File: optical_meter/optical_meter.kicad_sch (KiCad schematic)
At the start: 45 parts, among them J1 SFP+, J2 SFP+, J3 Conn_01x02_Pin, U2 FIN1002M5X, U3 FIN1001M5X

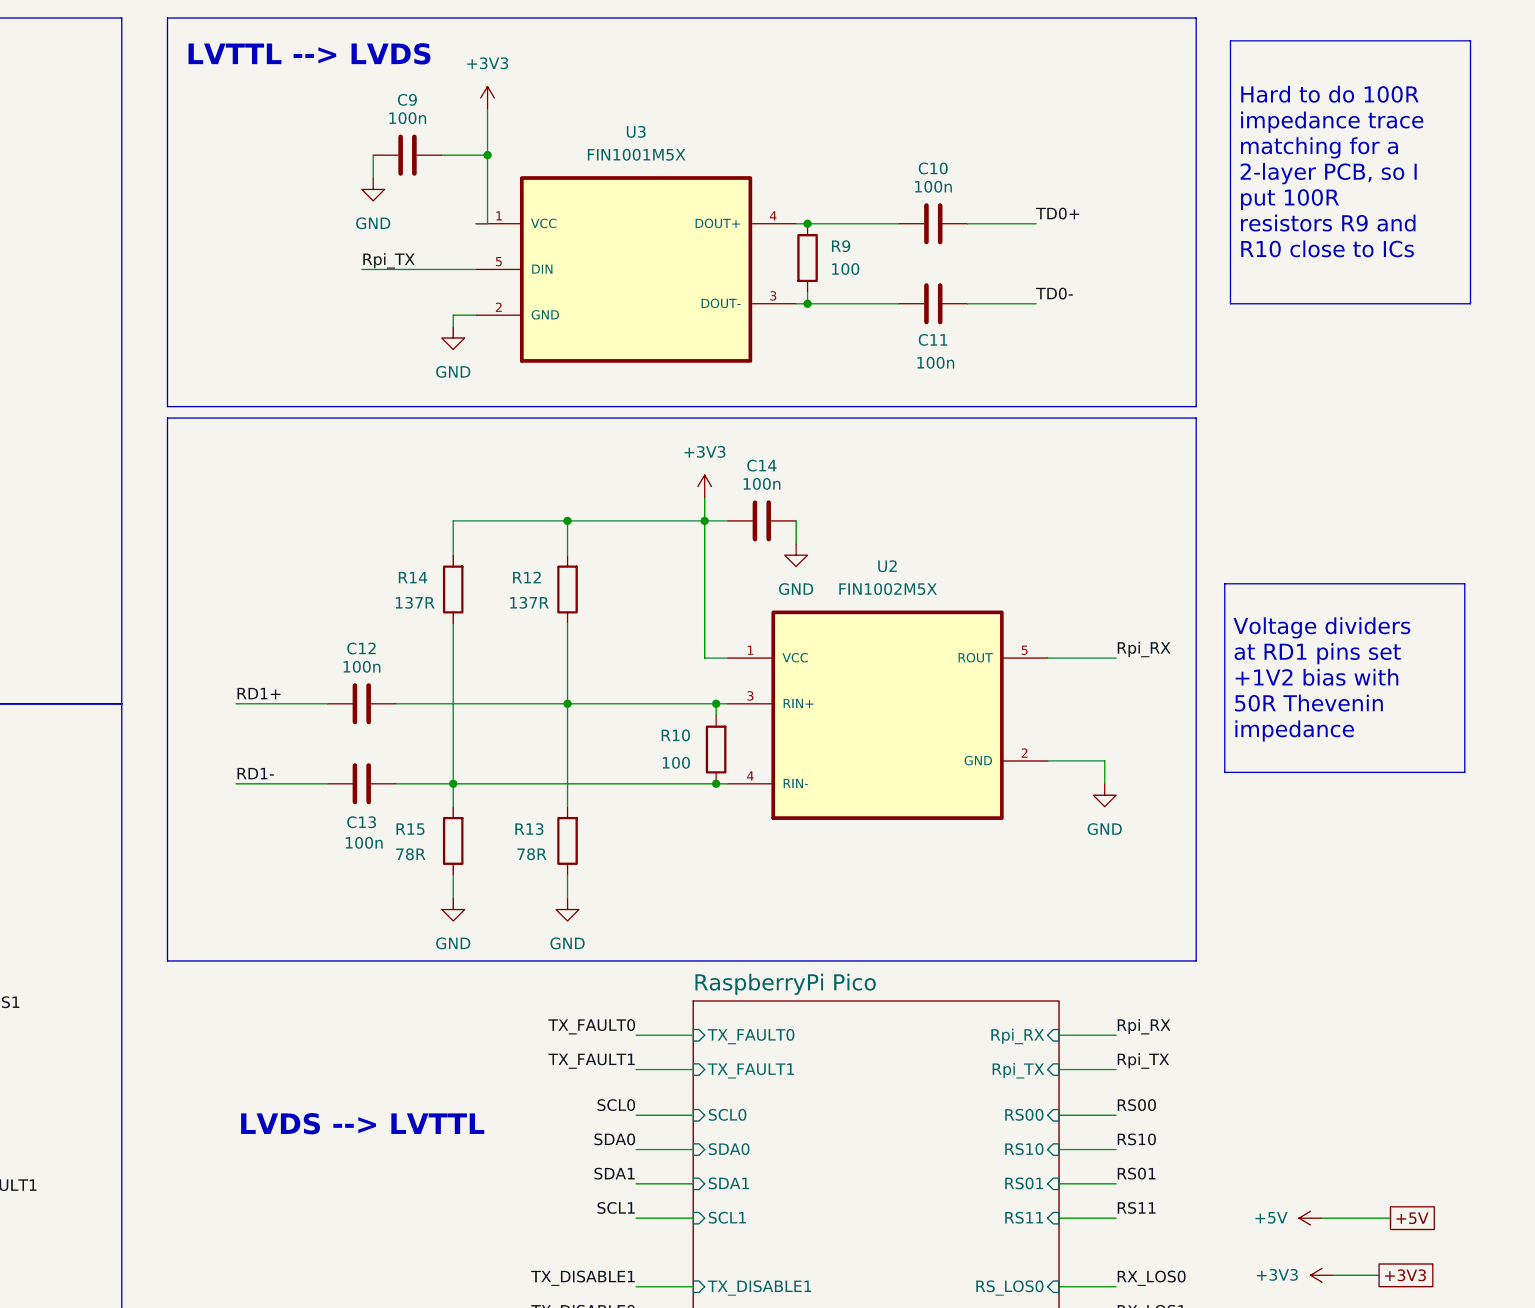
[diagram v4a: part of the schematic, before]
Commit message: Removing 100R termination Resistor R9 from TD0 lines
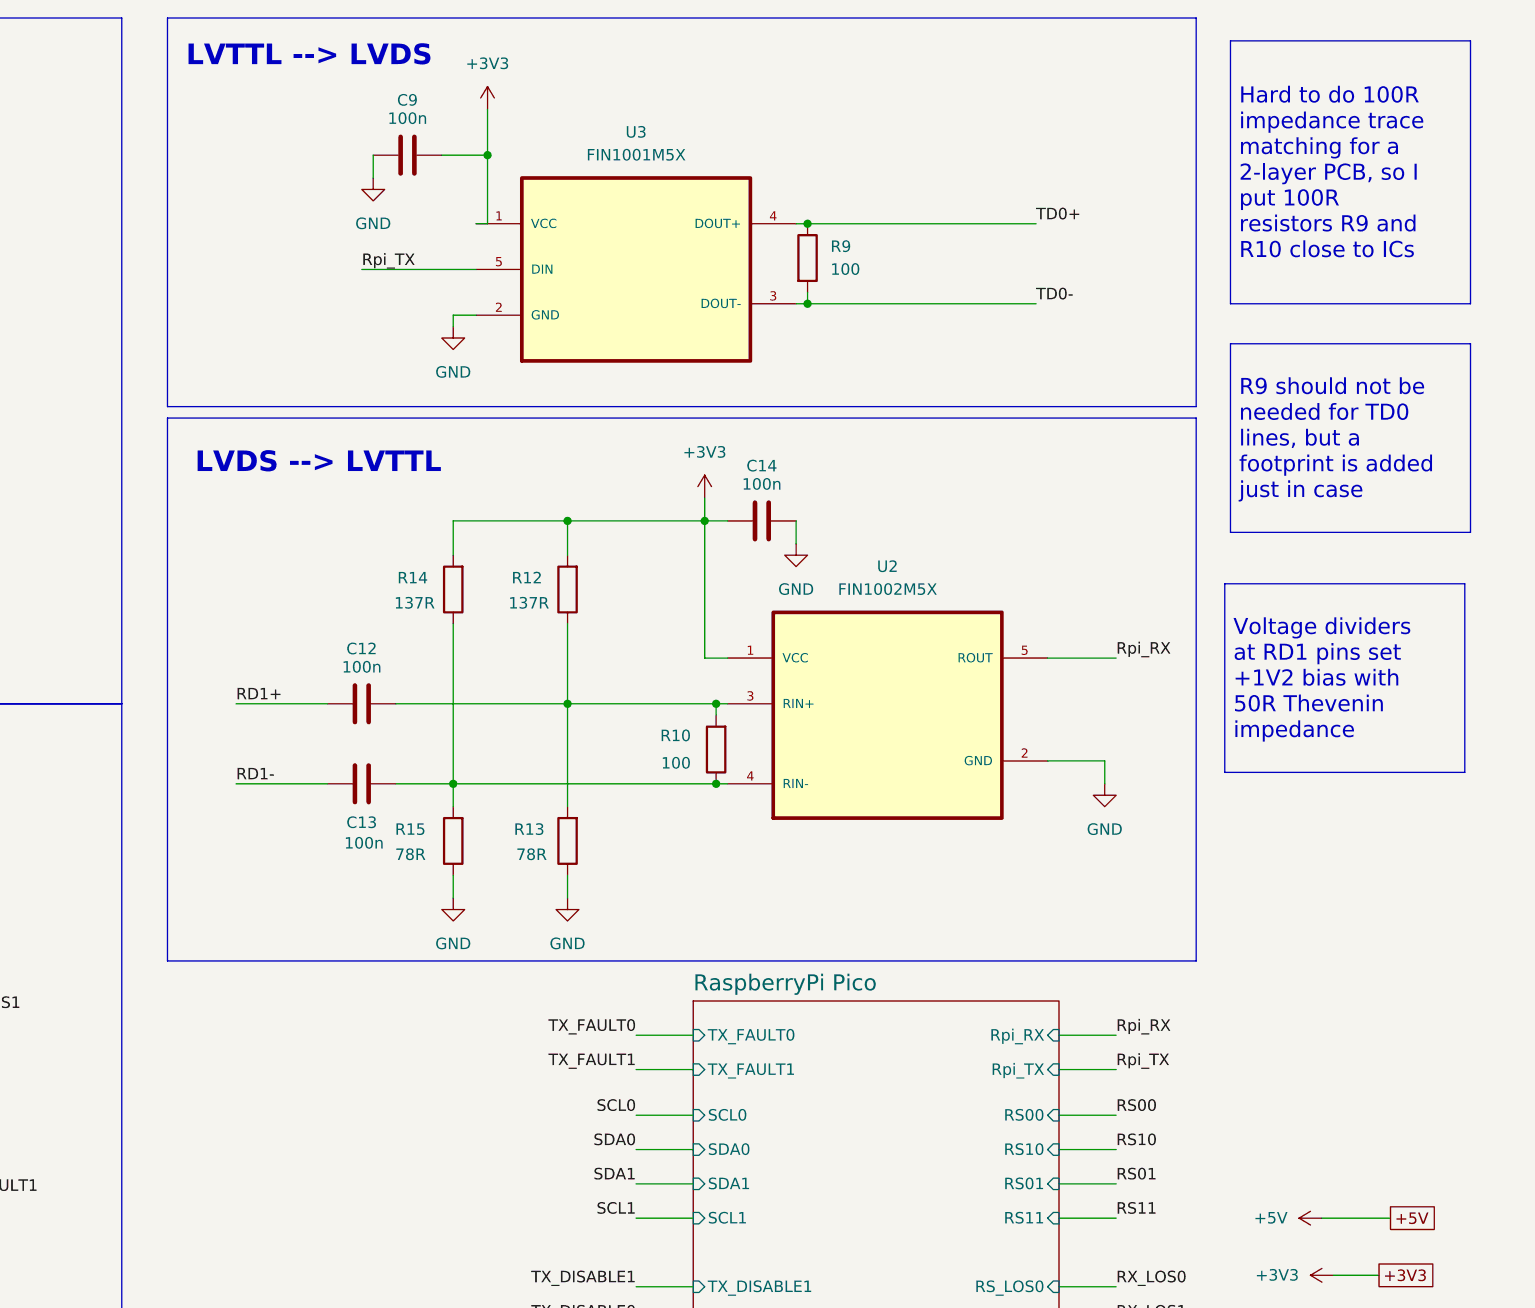
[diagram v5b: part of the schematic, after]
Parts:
- removed C10, C11: 100n, Capacitor_SMD:C_0603_1608Metric, symbol Device:C
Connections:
- net TD0+: now also R9.1, U3.4 (DOUT+)
- net TD0-: now also R9.2, U3.3 (DOUT-)
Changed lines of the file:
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@@
 	(text "LVDS --> LVTTL"
 		(exclude_from_sim no)
-		(at 158.75 135.89 0)
+		(at 153.924 62.23 0)
 		(effects
 			(font
@@
 		)
 	)
+	(text_box "R9 should not be needed for TD0 lines, but a footprint is added just in case"
+		(exclude_from_sim no)
+		(at 255.27 48.895 0)
+		(size 26.67 20.955)
+		(margins 0.9525 0.9525 0.9525 0.9525)
+		(stroke
+			(width 0)
+			(type solid)
+		)
+		(fill
+			(type color)
+			(color 241 253 255 1)
+		)
+		(effects
+			(font
+				(size 1.778 1.778)
+			)
+			(justify left)
+		)
+	)
 	(junction
 		(at 49.53 143.51)
@@
 	(wire
 		(pts
-			(xy 208.28 44.45) (xy 218.44 44.45)
+			(xy 208.28 44.45) (xy 233.68 44.45)
 		)
 		(stroke
@@
 	(wire
 		(pts
-			(xy 226.06 35.56) (xy 233.68 35.56)
-		)
-		(stroke
-			(width 0)
-			(type default)
-		)
-	)
-	(wire
-		(pts
 			(xy 54.61 97.79) (xy 54.61 102.87)
 		)
@@
 	(wire
 		(pts
-			(xy 208.28 35.56) (xy 218.44 35.56)
+			(xy 208.28 35.56) (xy 233.68 35.56)
 		)
 		(stroke
@@
 		)
 	)
-	(wire
-		(pts
-			(xy 226.06 44.45) (xy 233.68 44.45)
-		)
-		(stroke
-			(width 0)
-			(type default)
-		)
-	)
 	(label "RS00"
 		(at 46.99 64.77 0)
@@
 		(at 208.28 39.37 0)
 		(unit 1)
-		(exclude_from_sim no)
+		(exclude_from_sim yes)
 		(in_bom yes)
-		(on_board yes)
+		(on_board no)
 		(dnp no)
 		(fields_autoplaced yes)
@@
 	)
 	(symbol
-		(lib_id "Device:C")
-		(at 222.25 44.45 90)
-		(unit 1)
-		(exclude_from_sim no)
-		(in_bom yes)
-		(on_board yes)
-		(dnp no)
-		(property "Reference" "C11"
-			(at 222.25 48.514 90)
-			(effects
-				(font
-					(size 1.27 1.27)
-				)
-			)
-		)
-		(property "Value" "100n"
-			(at 222.504 51.054 90)
-			(effects
-				(font
-					(size 1.27 1.27)
-				)
-			)
-		)
-		(property "Footprint" "Capacitor_SMD:C_0603_1608Metric"
-			(at 226.06 43.4848 0)
-			(effects
-				(font
-					(size 1.27 1.27)
-				)
-				(hide yes)
-			)
-		)
-		(property "Datasheet" "~"
-			(at 222.25 44.45 0)
-			(effects
-				(font
-					(size 1.27 1.27)
-				)
-				(hide yes)
-			)
-		)
-		(property "Description" "Unpolarized capacitor"
-			(at 222.25 44.45 0)
-			(effects
-				(font
-					(size 1.27 1.27)
-				)
-				(hide yes)
-			)
-		)
-		(pin "1"
-		)
-		(pin "2"
-		)
-		(instances
-			(project "optical_meter"
-				(path "/329e6fb6-763d-4479-a593-6f78470800a1"
-					(reference "C11")
-					(unit 1)
-				)
-			)
-		)
-	)
-	(symbol
 		(lib_id "Device:LED")
 		(at 81.28 189.23 180)
@@
 					(unit 1)
 				)
-			)
-		)
-	)
-	(symbol
-		(lib_id "Device:C")
-		(at 222.25 35.56 90)
-		(unit 1)
-		(exclude_from_sim no)
-		(in_bom yes)
-		(on_board yes)
-		(dnp no)
-		(property "Reference" "C10"
-			(at 222.25 29.464 90)
-			(effects
-				(font
-					(size 1.27 1.27)
-				)
-			)
-		)
-		(property "Value" "100n"
-			(at 222.25 31.496 90)
-			(effects
-				(font
-					(size 1.27 1.27)
-				)
-			)
-		)
-		(property "Footprint" "Capacitor_SMD:C_0603_1608Metric"
-			(at 226.06 34.5948 0)
-			(effects
-				(font
-					(size 1.27 1.27)
-				)
-				(hide yes)
-			)
-		)
-		(property "Datasheet" "~"
-			(at 222.25 35.56 0)
-			(effects
-				(font
-					(size 1.27 1.27)
-				)
-				(hide yes)
-			)
-		)
-		(property "Description" "Unpolarized capacitor"
-			(at 222.25 35.56 0)
-			(effects
-				(font
-					(size 1.27 1.27)
-				)
-				(hide yes)
-			)
-		)
-		(pin "1"
-		)
-		(pin "2"
-		)
-		(instances
-			(project "optical_meter"
-				(path "/329e6fb6-763d-4479-a593-6f78470800a1"
-					(reference "C10")
-					(unit 1)
-				)

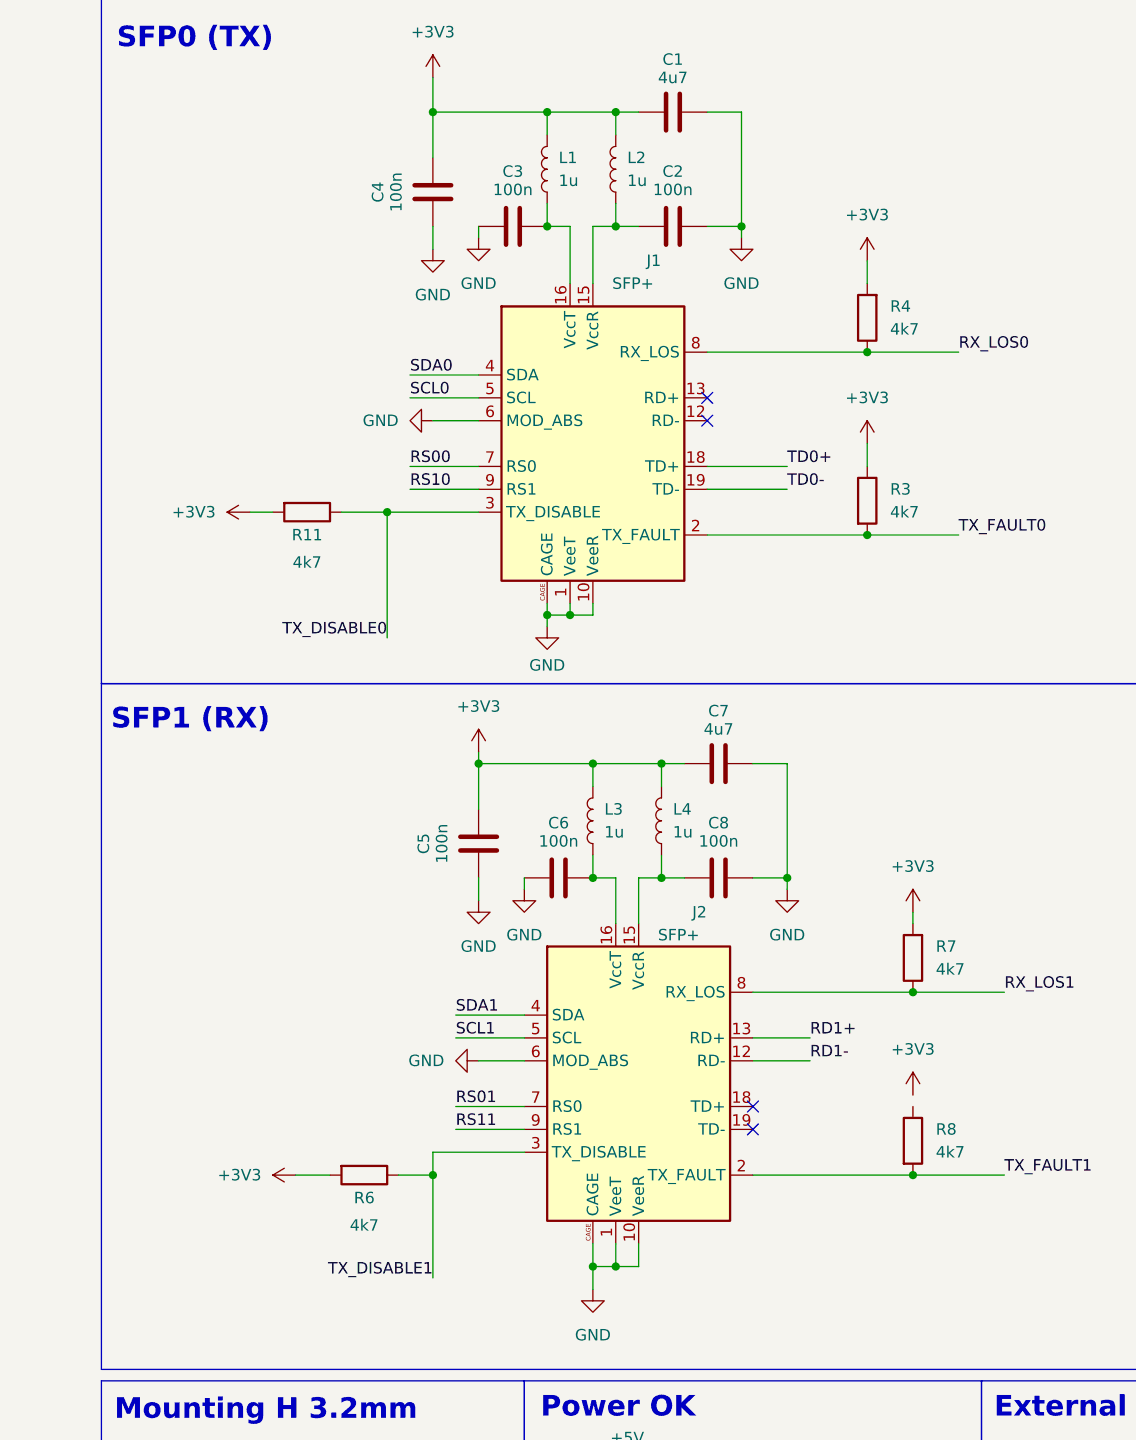
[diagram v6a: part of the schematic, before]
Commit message: Cosmetic changes to schematic - GND downwards, power rails upwards
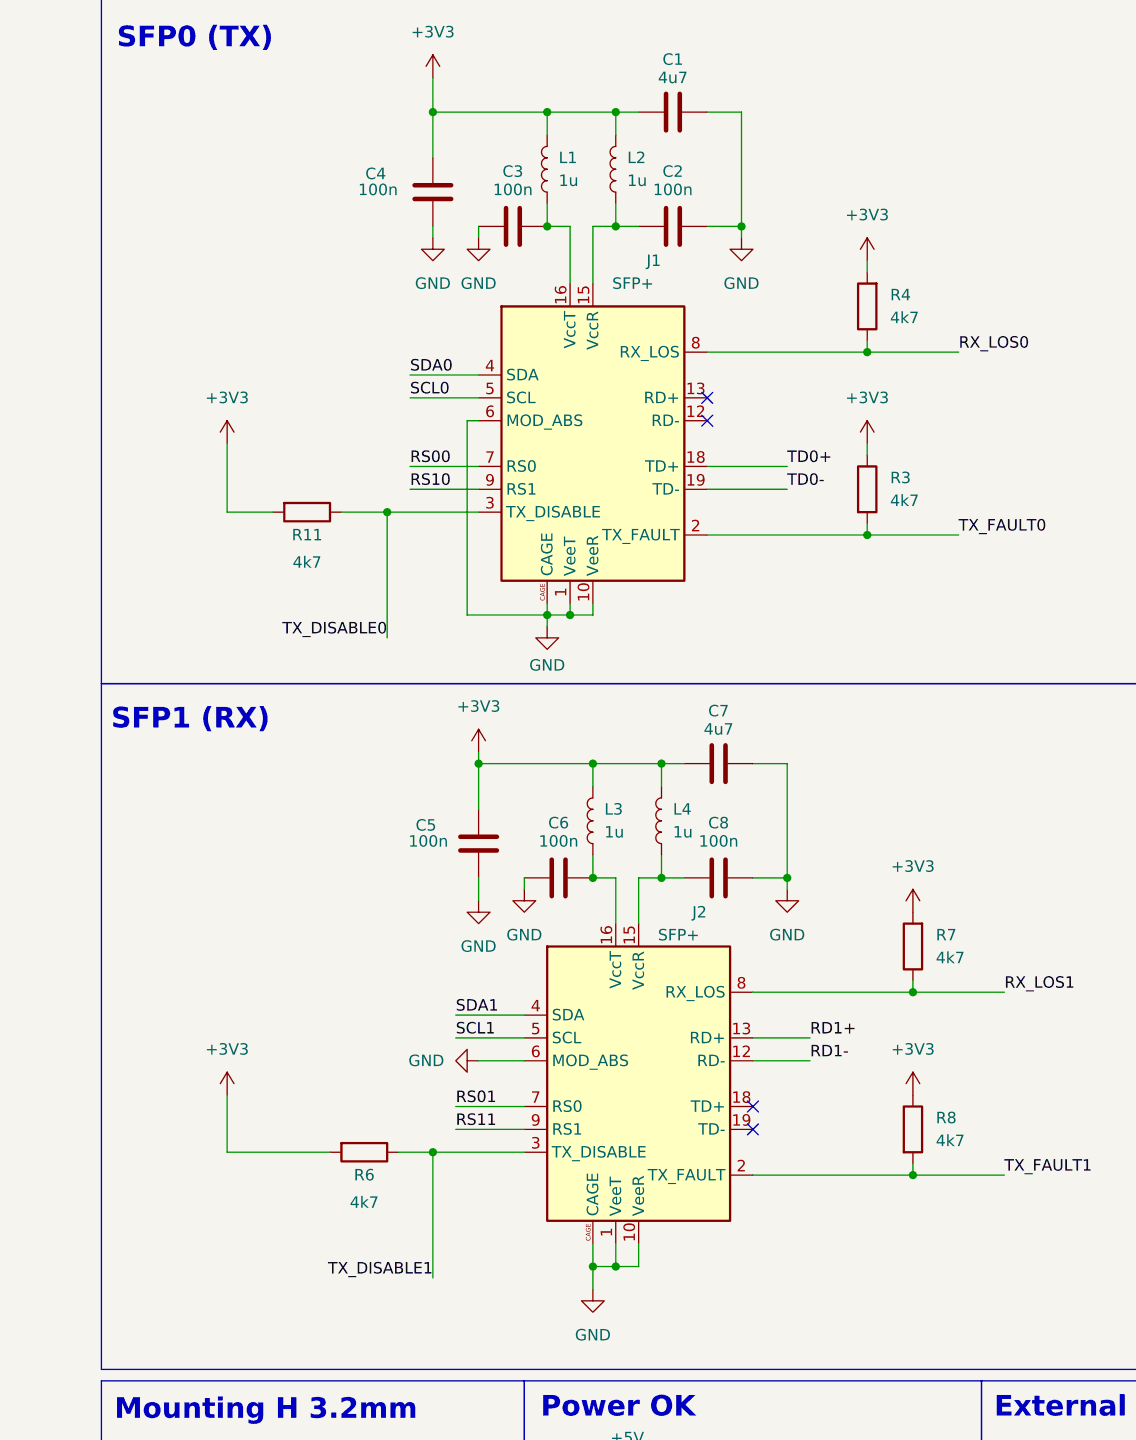
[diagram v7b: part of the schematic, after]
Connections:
- net +3V3: now also R8.1
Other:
- moved on the sheet: R3, R4, R6, R7, R8
